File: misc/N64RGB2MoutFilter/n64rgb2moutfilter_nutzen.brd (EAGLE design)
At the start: 129.7 x 29.5 mm, 70 parts

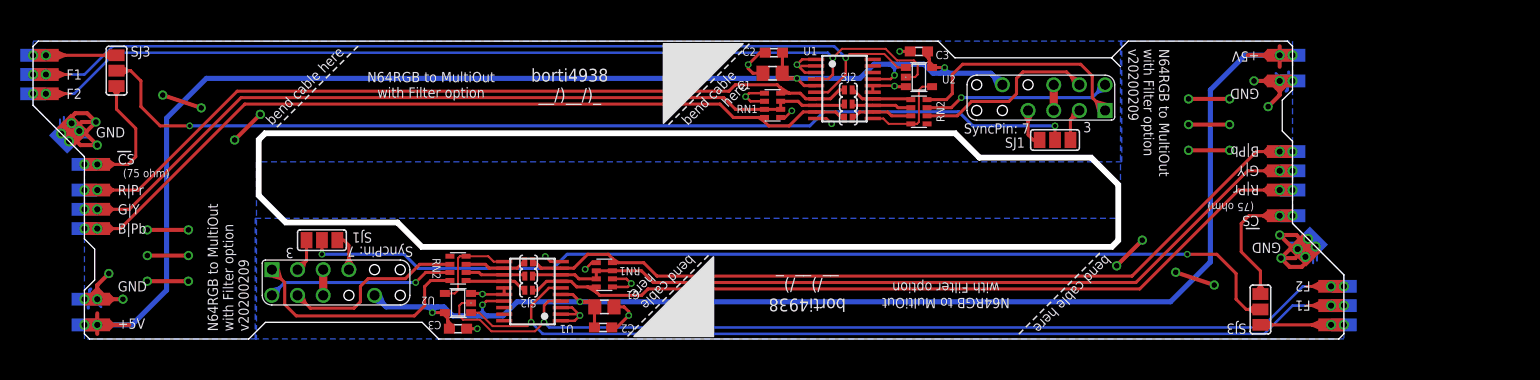
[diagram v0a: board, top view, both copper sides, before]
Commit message: adapt cable to fit with N64RGBv2.1
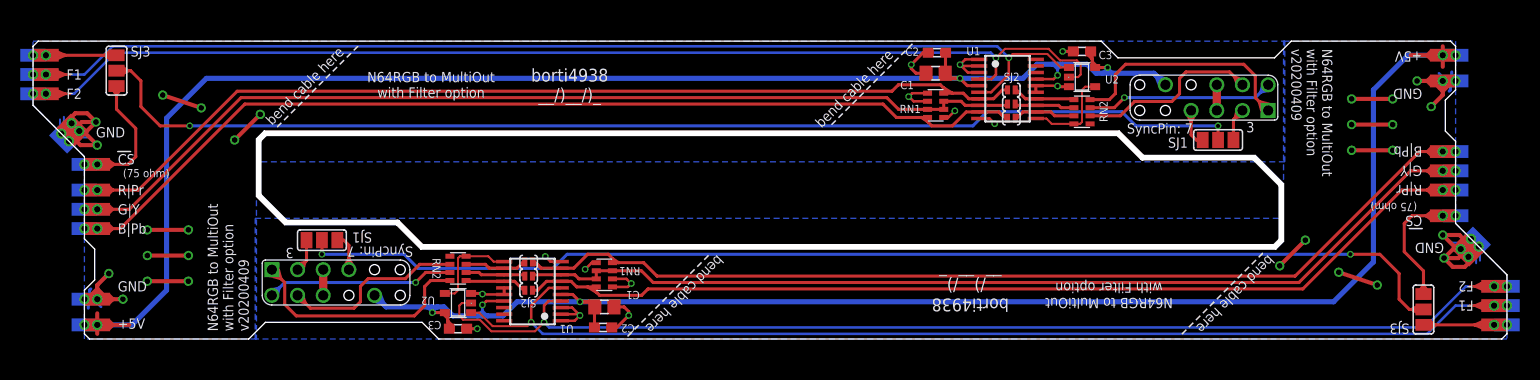
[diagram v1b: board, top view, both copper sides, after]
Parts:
- moved CS#3 16.1 mm to (144.5, 1.52)
- moved F7 16.1 mm to (144.5, 5.33)
- moved F8 16.1 mm to (144.5, 3.43)
- moved B/PB2 16.1 mm to (139.4, 18.7)
- moved B/PB3 16.1 mm to (140.7, 18.7)
- moved C1 16.1 mm to (89.3, 26.4)
- moved C2 16.1 mm to (89.4, 28.4)
- moved C3 16.1 mm to (103.8, 28.6)
- moved CS75#2 16.1 mm to (139.4, 12.3)
- moved CS75#3 16.1 mm to (140.7, 12.3)
- moved E$1 16.1 mm to (115.8, 24.0)
- moved G/Y2 16.1 mm to (139.4, 16.8)
- moved G/Y3 16.1 mm to (140.7, 16.8)
- moved P_GND10 16.1 mm to (140.7, 25.7)
- moved P_GND11 16.1 mm to (142.9, 9.91)
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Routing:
- net GREEN1: track 84.9 -> 101.0 mm
- net BLUE1: track 87.5 -> 103.6 mm
- net #CS.SEL1: track 100.6 -> 116.8 mm
- net RED: track 86.1 -> 102.2 mm
- net F4: track 101.6 -> 117.7 mm
- net F2: track 101.6 -> 117.7 mm
- net 5V1: track 139.2 -> 155.4 mm
- net #CS.SEL: track 100.6 -> 116.8 mm
- net RED1: track 86.1 -> 102.2 mm
- net GREEN: track 84.9 -> 101.0 mm
- net F3: track 98.8 -> 114.9 mm
- net F1: track 98.8 -> 114.9 mm
- net BLUE: track 87.5 -> 103.6 mm
- net 5V: track 139.2 -> 155.4 mm
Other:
- board size 129.7 x 29.5 mm -> 145.8 x 29.5 mm
- board text added: "N64RGB to MultiOut with Filter option v20200409"
- board text removed: "N64RGB to MultiOut with Filter option v20200209"
